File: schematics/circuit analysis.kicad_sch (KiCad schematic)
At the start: 2 parts

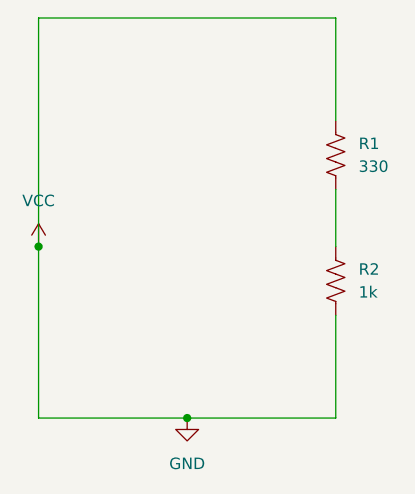
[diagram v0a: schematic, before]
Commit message: add voltage source
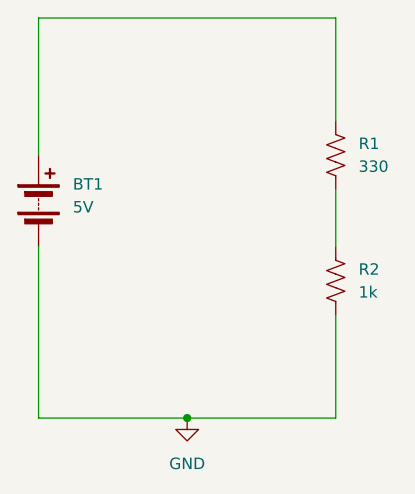
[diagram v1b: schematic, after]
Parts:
- added BT1: 5V, symbol Device:Battery
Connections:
- net GND: now also BT1.2 (-); no longer R1.1
- new net: BT1.1 (+), R1.1
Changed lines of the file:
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@@
 		(color 0 0 0 0)
 	)
-	(junction
-		(at 123.19 101.6)
-		(diameter 0)
-		(color 0 0 0 0)
-	)
 	(wire
 		(pts
@@
 	(wire
 		(pts
+			(xy 123.19 76.2) (xy 123.19 91.44)
+		)
+		(stroke
+			(width 0)
+			(type default)
+		)
+	)
+	(wire
+		(pts
 			(xy 156.21 120.65) (xy 139.7 120.65)
 		)
@@
 			(width 0)
 			(type default)
-		)
-	)
-	(wire
-		(pts
-			(xy 123.19 76.2) (xy 123.19 101.6)
-		)
-		(stroke
-			(width 0)
-			(type default)
-		)
-	)
-	(symbol
-		(lib_id "power:VCC")
-		(at 123.19 101.6 0)
-		(unit 1)
-		(exclude_from_sim no)
-		(in_bom yes)
-		(on_board yes)
-		(dnp no)
-		(fields_autoplaced yes)
-		(property "Reference" "#PWR01"
-			(at 123.19 105.41 0)
-			(effects
-				(font
-					(size 1.27 1.27)
-				)
-				(hide yes)
-			)
-		)
-		(property "Value" "VCC"
-			(at 123.19 96.52 0)
-			(effects
-				(font
-					(size 1.27 1.27)
-				)
-			)
-		)
-		(property "Footprint" ""
-			(at 123.19 101.6 0)
-			(effects
-				(font
-					(size 1.27 1.27)
-				)
-				(hide yes)
-			)
-		)
-		(property "Datasheet" ""
-			(at 123.19 101.6 0)
-			(effects
-				(font
-					(size 1.27 1.27)
-				)
-				(hide yes)
-			)
-		)
-		(property "Description" "Power symbol creates a global label with name \"VCC\""
-			(at 123.19 101.6 0)
-			(effects
-				(font
-					(size 1.27 1.27)
-				)
-				(hide yes)
-			)
-		)
-		(pin "1"
-		)
-		(instances
-			(project ""
-				(path "/cee36828-924a-462d-b551-94ce78735ad3"
-					(reference "#PWR01")
-					(unit 1)
-				)
-			)
 		)
 	)
@@
 					(unit 1)
 				)
+			)
+		)
+	)
+	(symbol
+		(lib_id "Device:Battery")
+		(at 123.19 96.52 0)
+		(unit 1)
+		(exclude_from_sim no)
+		(in_bom yes)
+		(on_board yes)
+		(dnp no)
+		(fields_autoplaced yes)
+		(property "Reference" "BT1"
+			(at 127 94.6784 0)
+			(effects
+				(font
+					(size 1.27 1.27)
+				)
+				(justify left)
+			)
+		)
+		(property "Value" "5V"
+			(at 127 97.2184 0)
+			(effects
+				(font
+					(size 1.27 1.27)
+				)
+				(justify left)
+			)
+		)
+		(property "Footprint" ""
+			(at 123.19 94.996 90)
+			(effects
+				(font
+					(size 1.27 1.27)
+				)
+				(hide yes)
+			)
+		)
+		(property "Datasheet" "~"
+			(at 123.19 94.996 90)
+			(effects
+				(font
+					(size 1.27 1.27)
+				)
+				(hide yes)
+			)
+		)
+		(property "Description" "Multiple-cell battery"
+			(at 123.19 96.52 0)
+			(effects
+				(font
+					(size 1.27 1.27)
+				)
+				(hide yes)
+			)
+		)
+		(pin "1"
+		)
+		(pin "2"
+		)
+		(instances
+			(project ""
+				(path "/cee36828-924a-462d-b551-94ce78735ad3"
+					(reference "BT1")
+					(unit 1)
+				)
